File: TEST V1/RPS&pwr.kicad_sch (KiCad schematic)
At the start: 42 parts, among them J10 Conn_01x01_Pin, J12 Conn_01x01_Pin, J7 Conn_01x01_Pin, J8 Conn_01x01_Pin, J9 Conn_01x01_Pin, Q2 PMOS, U11 TVS1800DRV, U12 TPS54202DDC, U13 MCP4725xxx-xCH, U6 LM2596T-5

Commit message: updated RPS schematic
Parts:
- U13: value MCP4725xxx-xCH -> MCP4725A2T-ECH
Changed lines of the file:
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@@
 			)
 		)
-		(property "Value" "MCP4725xxx-xCH"
+		(property "Value" "MCP4725A2T-ECH"
 			(at 189.484 110.998 0)
 			(effects

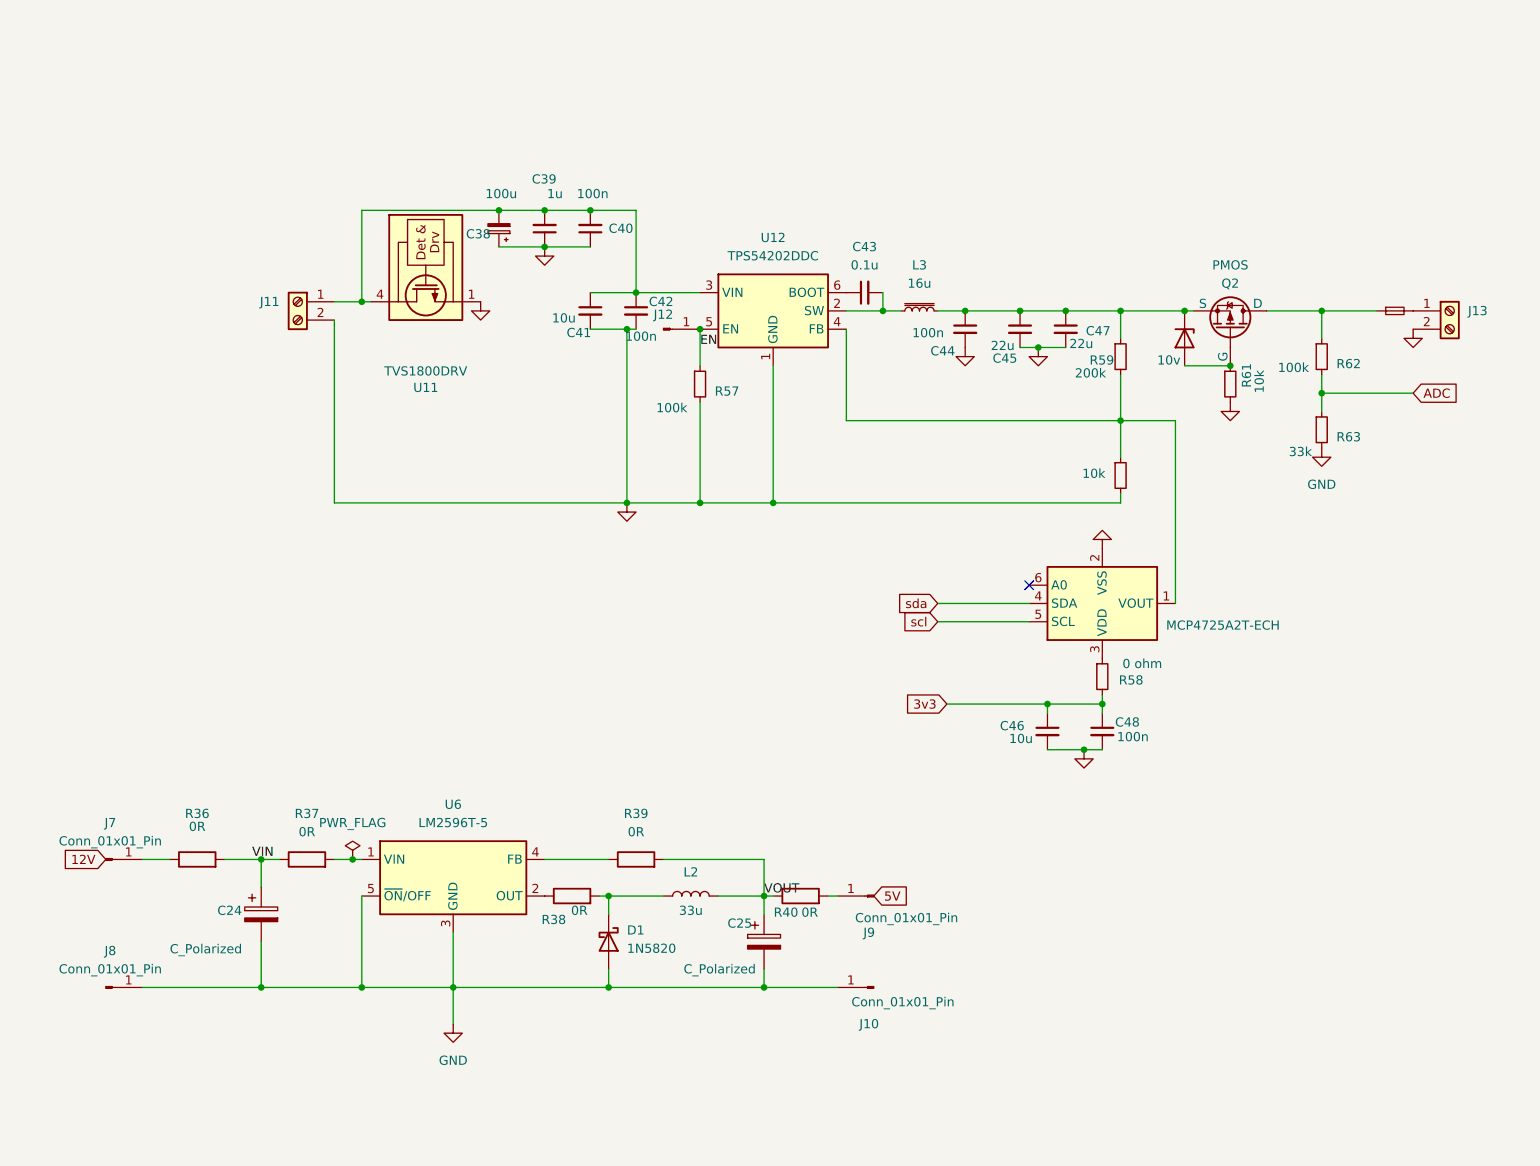
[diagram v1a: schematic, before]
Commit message: updated schematic of FG
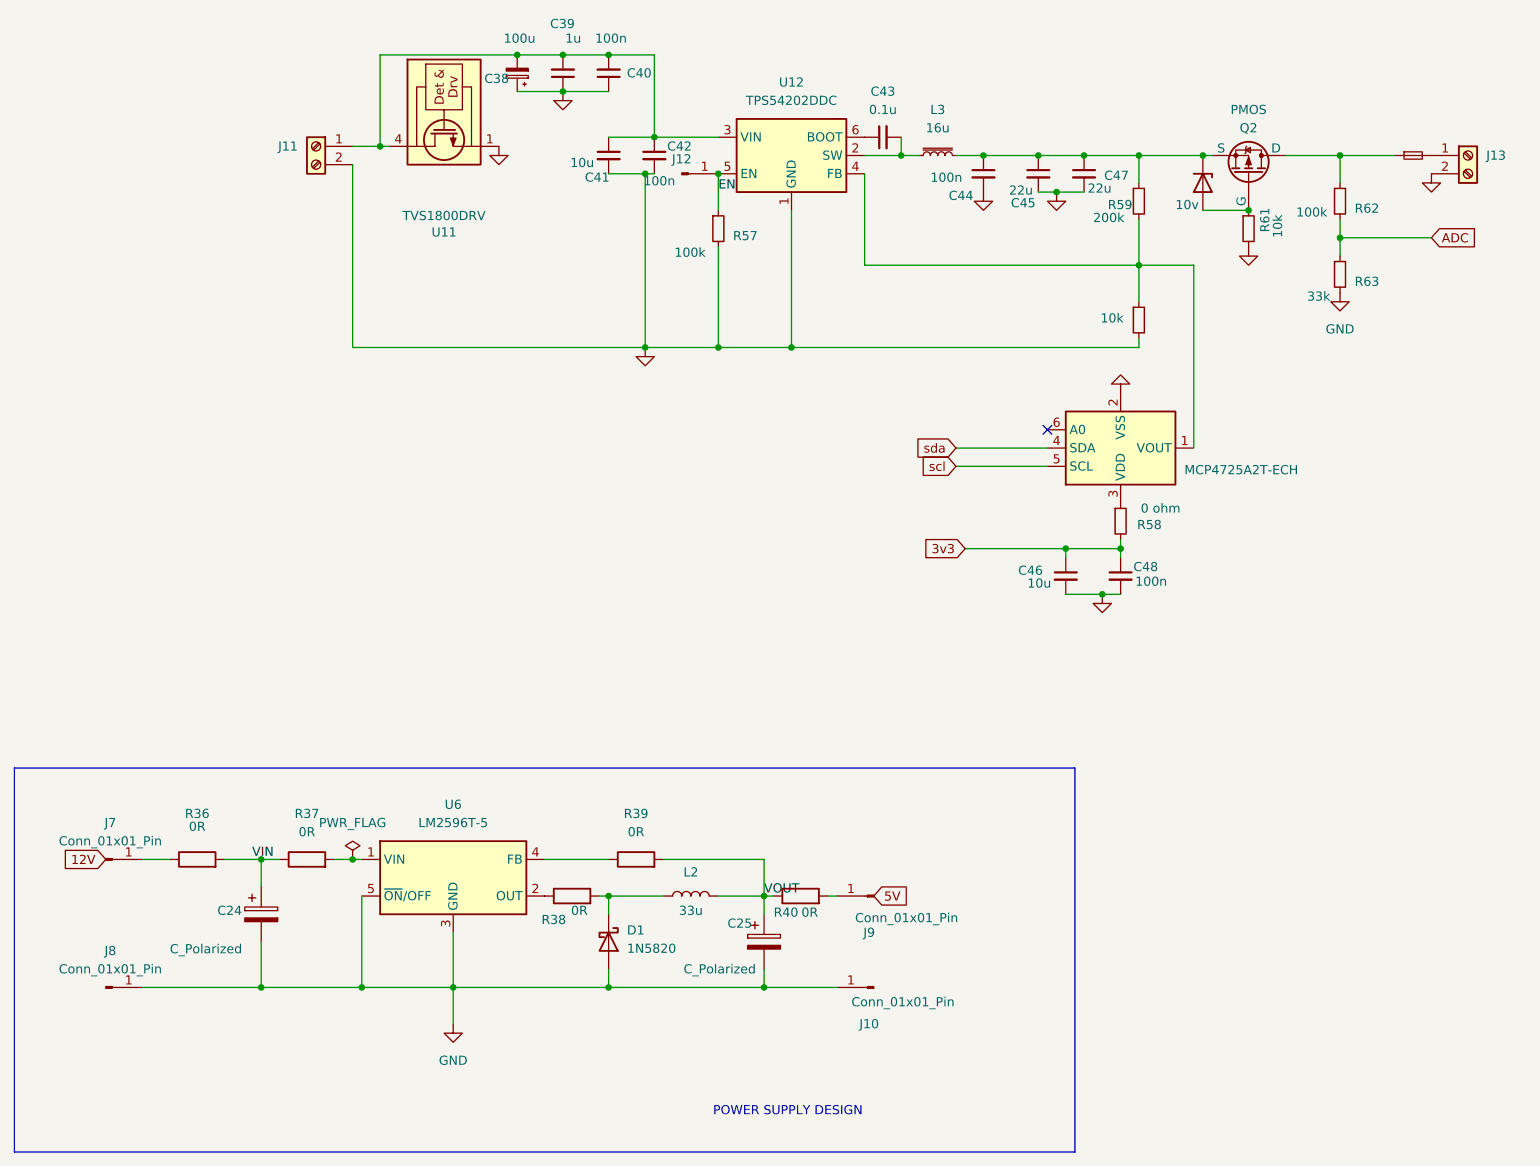
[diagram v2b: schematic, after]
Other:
- note added: "POWER SUPPLY DESIGN"
- moved on the sheet: C38, C39, C40, C41, C42, C43, C44, C45, C46, C47, C48, J11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

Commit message: updated RPS sch
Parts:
- removed C38: 100u, Capacitor_SMD:CP_Elec_6.3x8, symbol Device:C_Polarized_Small
- removed C41: 10u, Capacitor_SMD:C_0603_1608Metric_Pad1.08x0.95mm_HandSolder, symbol Device:C_Small
- removed C48: 100n, Capacitor_SMD:C_0603_1608Metric_Pad1.08x0.95mm_HandSolder, symbol Device:C_Small
- removed D3: 10v, Diode_SMD:D_SOD-123, symbol Device:D_Zener
- removed F2: Fuse_Small, Fuse:Fuse_1206_3216Metric, symbol Device:Fuse_Small
- removed J11: ~, TerminalBlock_Phoenix:TerminalBlock_Phoenix_MKDS-1,5-2-5.08_1x02_P5.08mm_Horizontal, symbol Connector:Screw_Terminal_01x02
- removed J12: Conn_01x01_Pin, Connector_PinHeader_2.54mm:PinHeader_1x01_P2.54mm_Vertical, symbol Connector:Conn_01x01_Pin
- removed Q2: PMOS, Package_TO_SOT_SMD:SOT-223-3_TabPin2, symbol Simulation_SPICE:PMOS
- removed R37, R39: 0R, Resistor_SMD:R_0603_1608Metric_Pad0.98x0.95mm_HandSolder, symbol Device:R
- removed R58: 0 ohm, Resistor_SMD:R_0805_2012Metric_Pad1.20x1.40mm_HandSolder, symbol Device:R_Small
- removed R59: 200k, Resistor_SMD:R_0603_1608Metric_Pad0.98x0.95mm_HandSolder, symbol Device:R_Small
- removed R60, R61: 10k, Resistor_SMD:R_0603_1608Metric_Pad0.98x0.95mm_HandSolder, symbol Device:R_Small
- removed R62: 100k, Resistor_SMD:R_0603_1608Metric_Pad0.98x0.95mm_HandSolder, symbol Device:R_Small
- removed R63: 33k, Resistor_SMD:R_0603_1608Metric_Pad0.98x0.95mm_HandSolder, symbol Device:R_Small
- removed U11: TVS1800DRV, Diode_SMD:D_SMA, symbol Power_Protection:TVS1800DRV
- removed U12: TPS54202DDC, Package_TO_SOT_SMD:SOT-23-6, symbol Regulator_Switching:TPS54202DDC
- removed U13: MCP4725A2T-ECH, Package_TO_SOT_SMD:SOT-23-6, symbol Analog_DAC:MCP4725xxx-xCH
- added C36: 100u, Capacitor_SMD:CP_Elec_6.3x8, symbol Device:C_Polarized_Small
- added C37: 1u, Capacitor_SMD:C_0603_1608Metric_Pad1.08x0.95mm_HandSolder, symbol Device:C_Small
- added C38: 100n, Capacitor_SMD:C_0603_1608Metric_Pad1.08x0.95mm_HandSolder, symbol Device:C_Small
- added D3: D_TVS, Diode_SMD:D_SMA_Handsoldering, symbol Device:D_TVS
- added D4: 10v, Diode_SMD:D_SOD-123, symbol Device:D_Zener
- added F1: Fuse_Small, Fuse:Fuse_1206_3216Metric, symbol Device:Fuse_Small
- added J12: ~, TerminalBlock_Phoenix:TerminalBlock_Phoenix_MKDS-1,5-2-5.08_1x02_P5.08mm_Horizontal, symbol Connector:Screw_Terminal_01x02
- added Q1: PMOS, Package_TO_SOT_SMD:SOT-223-3_TabPin2, symbol Simulation_SPICE:PMOS
- added R51: 0 ohm, Resistor_SMD:R_0805_2012Metric_Pad1.20x1.40mm_HandSolder, symbol Device:R_Small
- added R53: 200k, Resistor_SMD:R_0603_1608Metric_Pad0.98x0.95mm_HandSolder, symbol Device:R_Small
- added R54, R55: 10k, Resistor_SMD:R_0603_1608Metric_Pad0.98x0.95mm_HandSolder, symbol Device:R_Small
- added R56: 100k, Resistor_SMD:R_0603_1608Metric_Pad0.98x0.95mm_HandSolder, symbol Device:R_Small
- added U11: MCP4725xxx-xCH, Package_TO_SOT_SMD:SOT-23-6, symbol Analog_DAC:MCP4725xxx-xCH
- added U9: TPS54202DDC, Package_TO_SOT_SMD:SOT-23-6, symbol Regulator_Switching:TPS54202DDC
- C39: value 1u -> 10u
- C42: value 100n -> 0.1u
- C43: value 0.1u -> 100n
- C44: value 100n -> 22u; footprint Capacitor_SMD:C_0603_1608Metric_Pad1.08x0.95mm_HandSolder -> Capacitor_SMD:C_0805_2012Metric_Pad1.18x1.45mm_HandSolder
- C45: value 22u -> 10u; footprint Capacitor_SMD:C_0805_2012Metric_Pad1.18x1.45mm_HandSolder -> Capacitor_SMD:C_0603_1608Metric_Pad1.08x0.95mm_HandSolder
- C46: value 10u -> 22u; footprint Capacitor_SMD:C_0603_1608Metric_Pad1.08x0.95mm_HandSolder -> Capacitor_SMD:C_0805_2012Metric_Pad1.18x1.45mm_HandSolder
- C47: value 22u -> 100n; footprint Capacitor_SMD:C_0805_2012Metric_Pad1.18x1.45mm_HandSolder -> Capacitor_SMD:C_0603_1608Metric_Pad1.08x0.95mm_HandSolder
- R57: value 100k -> 33k
- renumbered C24 to C35, C25 to C41, D1 to D2, J7 to J10, J8 to J11, J9 to J14, J10 to J15, R36 to R47, R38 to R49, R40 to R52, U6 to U10
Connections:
- net EN is gone; now on net ADC: R57.1
- net 3v3: now also C45.1, C47.1, R51.2; no longer C46.1
- net ADC: now also R56.2
- net GND: now also C39.2, C40.2, C43.2, C36.1, C37.1, C38.1, D3.2 (A2), J12.2 (Pin_2), R54.2, R55.2, U11.2 (VSS), U9.1 (GND); no longer C39.1, C40.1, C42.2
- net VIN: now also U10.1 (VIN)
- net VOUT: now also U10.4 (FB)
- net at C43.1: now also C44.1, C46.1, L3.2, D4.1 (K), Q1.3 (S), R53.1
- net at L3.1: now also C42.2, U9.2 (SW); no longer C43.2
- net at J13.1 (Pin_1): now also F1.2
- new net: C36.2, C37.2, C38.2, C39.1, C40.1, D3.1 (A1), J12.1 (Pin_1), U9.3 (VIN)
- new net: F1.1, Q1.1 (D), R56.1
- new net: D4.2 (A), Q1.2 (G), R55.1
- new net: R53.2, R54.1, U11.1 (VOUT), U9.4 (FB)
- new net: R51.1, U11.3 (VDD)
- new net: C42.1, U9.6 (BOOT)
- new net I2C_SCL: U11.5 (SCL)
- new net I2C_SDA: U11.4 (SDA)
- new net TPS_EN: U9.5 (EN)
